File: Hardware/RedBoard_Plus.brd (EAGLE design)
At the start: 68.6 x 58.4 mm, 179 parts, among them IC3 LM1117, J1 DNP, J2 ISP, J3 5.5x2.1mm Barrel, J4 QWIIC_RIGHT_ANGLE, J5 USB Female Type C Connector, Q1 20V/4.2A/52mΩ/1.4W, Q2 310mA/60V/1.6Ω, Q3 310mA/60V/1.6Ω, U1 CH340G, U3 3.3V, U4 ATMEGA328P_TQFP, Y1 16MHz, Y2 12MHz

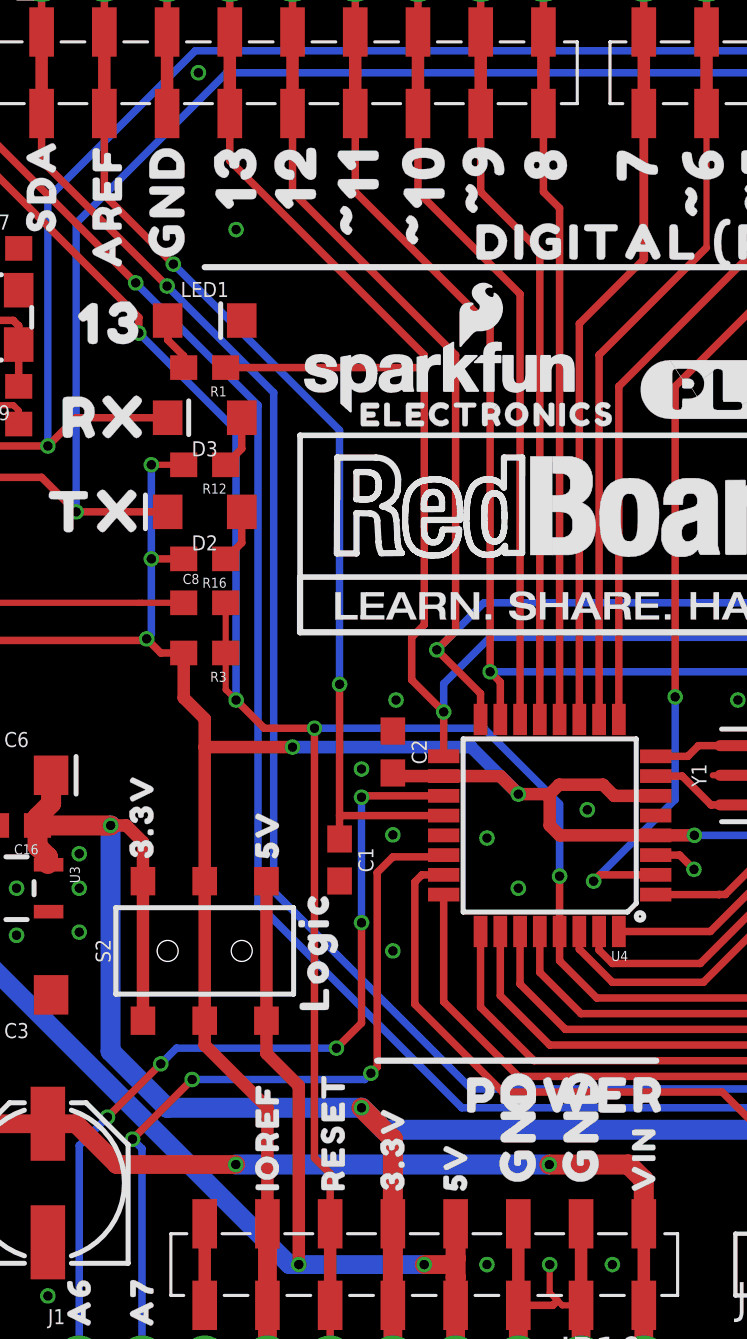
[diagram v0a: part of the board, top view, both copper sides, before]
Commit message: Update "GND" Buzzard labels
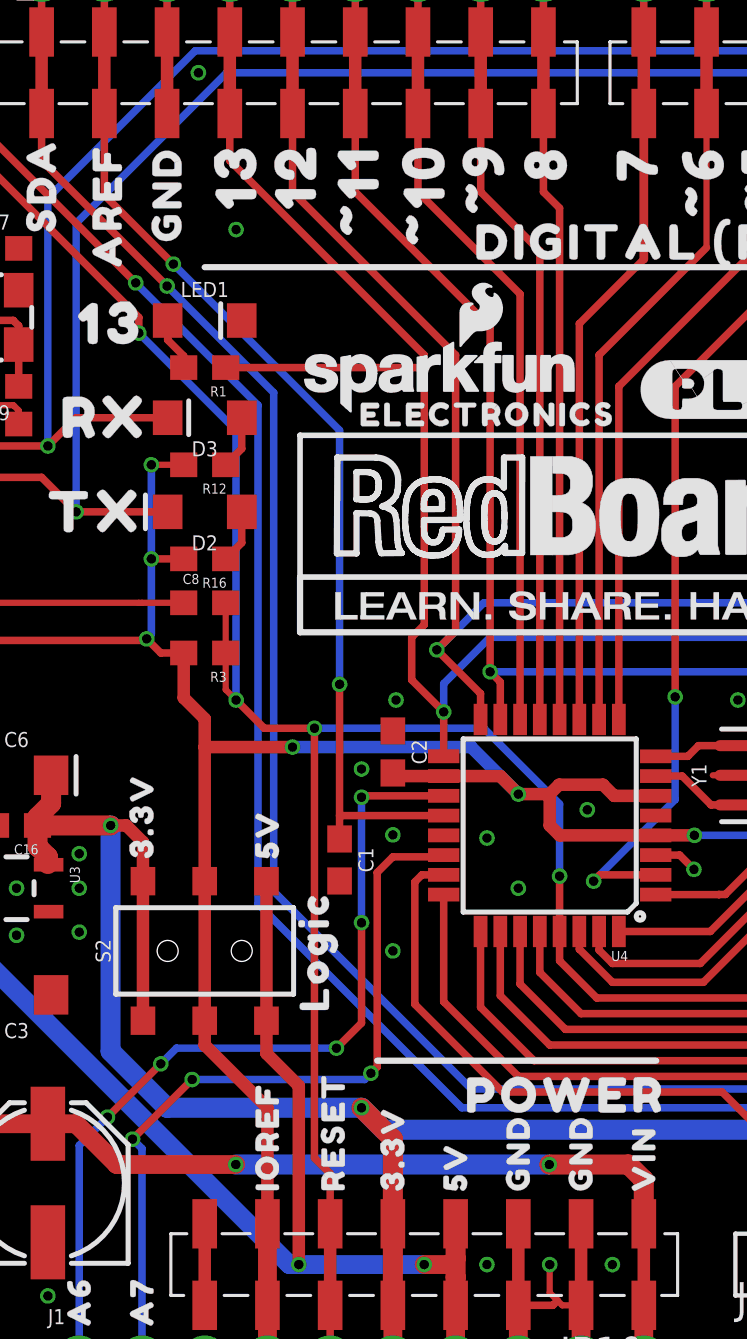
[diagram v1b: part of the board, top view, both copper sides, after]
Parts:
- removed U$21, U$91, U$92: (no value), output:_GND0
- added U$107, U$85: (no value), output:_GND_0
- added U$42: (no value), output:_GND0
- U$99: device output:GND0 -> output:_GND_0
- moved U$99 38.1 mm to (40.6, 9.53), flipped to the bottom, turned to 270 degrees
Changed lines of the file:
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@@
 <?xml version="1.0" encoding="utf-8"?>
 <!DOCTYPE eagle SYSTEM "eagle.dtd">
-<eagle version="9.5.2">
+<eagle version="9.6.2">
 <drawing>
 <settings>
-<setting alwaysvectorfont="no"/>
+<setting alwaysvectorfont="yes"/>
 <setting keepoldvectorfont="yes"/>
 <setting verticaltext="up"/>
@@
 <element name="U$2" library="output" package="_D#0" value="" x="6.096" y="42.799" smashed="yes" rot="MR0"/>
 <element name="U$10" library="output" package="G0" value="" x="5.207" y="39.243" smashed="yes" rot="MR0"/>
-<element name="U$21" library="output" package="_GND0" value="" x="26.416" y="57.658" smashed="yes" rot="MR270"/>
 <element name="FD1" library="SparkFun-Aesthetics" package="FIDUCIAL-1X2" value="FIDUCIAL1X2" x="11.43" y="54.61" smashed="yes" rot="MR0"/>
 <element name="FD2" library="SparkFun-Aesthetics" package="FIDUCIAL-1X2" value="FIDUCIAL1X2" x="66.04" y="13.97" smashed="yes" rot="MR0"/>
@@
 <element name="U$89" library="output" package="_A00" value="" x="50.8" y="7.62" smashed="yes" rot="MR270"/>
 <element name="U$90" library="output" package="_VIN0" value="" x="45.72" y="8.89" smashed="yes" rot="MR270"/>
-<element name="U$91" library="output" package="_GND0" value="" x="43.053" y="9.652" smashed="yes" rot="MR270"/>
-<element name="U$92" library="output" package="_GND0" value="" x="40.64" y="9.652" smashed="yes" rot="MR270"/>
 <element name="U$93" library="output" package="_5V0" value="" x="38.1" y="7.62" smashed="yes" rot="MR270"/>
 <element name="U$94" library="output" package="_3#3V0" value="" x="35.56" y="10.16" smashed="yes" rot="MR270"/>
@@
 <element name="U$98" library="output" package="_A70" value="" x="25.4" y="7.62" smashed="yes" rot="MR270"/>
 <element name="U$13" library="output" package="_RESET0" value="" x="-0.762" y="48.387" smashed="yes"/>
-<element name="U$99" library="output" package="GND0" value="" x="26.416" y="44.831" smashed="yes" rot="R90"/>
 <element name="U$18" library="output" package="_AREF0" value="" x="24.003" y="44.196" smashed="yes" rot="R90"/>
 <element name="U$19" library="output" package="_SCL0" value="" x="18.796" y="45.72" smashed="yes" rot="R90"/>
@@
 <element name="U$106" library="output" package="#A5#0" value="" x="62.611" y="14.732" smashed="yes" rot="MR0"/>
 <element name="U$11" library="output" package="LOGIC0" value="" x="32.385" y="14.478" smashed="yes" rot="R90"/>
+<element name="U$42" library="output" package="_GND0" value="" x="26.416" y="45.212" smashed="yes" rot="R90"/>
+<element name="U$85" library="output" package="_GND_0" value="" x="26.416" y="57.785" smashed="yes" rot="MR270"/>
+<element name="U$99" library="output" package="_GND_0" value="" x="40.64" y="9.525" smashed="yes" rot="MR270"/>
+<element name="U$107" library="output" package="_GND_0" value="" x="43.18" y="9.525" smashed="yes" rot="MR270"/>
 </elements>
 <signals>

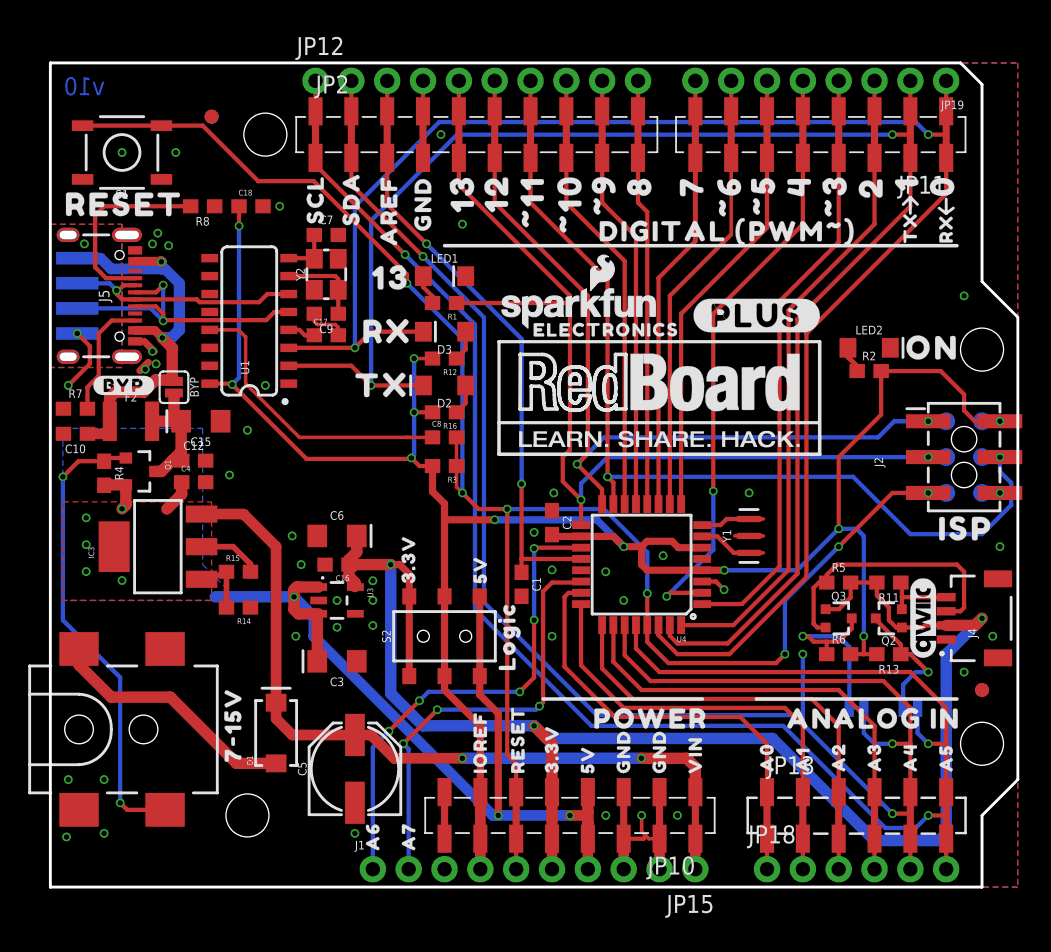
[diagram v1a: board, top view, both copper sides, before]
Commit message: Follow Up review changes
Added Qwiic logo device to schematic
Switch RXO/TXI signals at CH340G. Switched the order of LEDs as well
Updated headers to use current library parts
Updated ISP header sch symbol to use COPI/CIPO
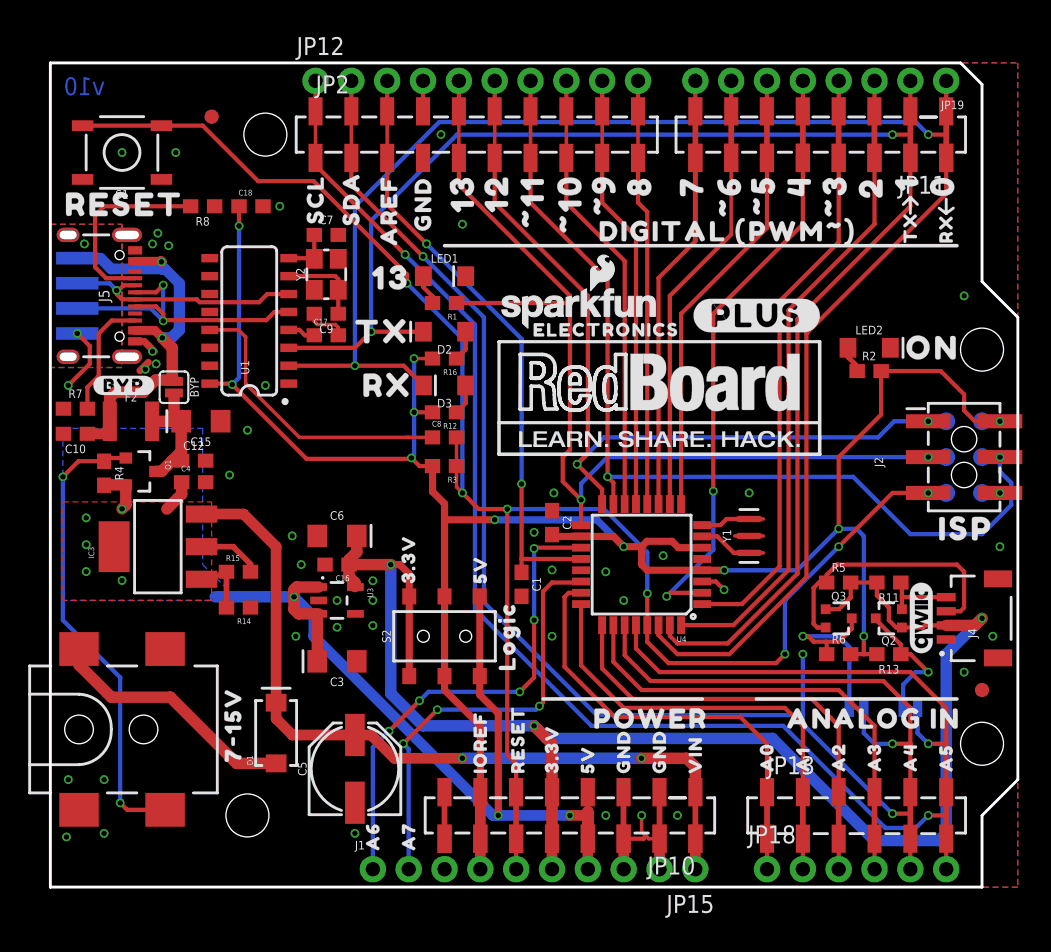
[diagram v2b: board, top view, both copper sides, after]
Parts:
- removed U$9: (no value), Labels:QWIIC_COPYRIGHT_SMALL
- added LOGO1: QWIIC_LOGO_5MM, SparkFun-Aesthetics:QWIIC_5MM
- JP10, JP11: device SparkFun-Connectors:1X08_SMD_COMBINED@1 -> SparkFun-Connectors:1X08_SMD_COMBINED
- JP15: device SparkFun-Connectors:1X08_NO_SILK@1 -> SparkFun-Connectors:1X08_NO_SILK
- JP18: device SparkFun-Connectors:1X06_NO_SILK@1 -> SparkFun-Connectors:1X06_NO_SILK
- JP2: value M10SMD_COMBO -> (none)
- moved R12 3.81 mm to (27.9, 33.7)
- moved R16 3.81 mm to (27.9, 37.5)
- moved D2 3.81 mm to (27.9, 39.4)
- moved D3 3.81 mm to (27.9, 35.6)
- moved U$40 3.81 mm to (19.8, 39.4)
- moved U$41 3.81 mm to (20.3, 35.6)
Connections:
- net !RESET: now also JP10.6; no longer JP10.6A, JP10.6B
- net 3.3V: now also JP10.5; no longer JP10.5A, JP10.5B
- net 5V: now also JP10.4; no longer JP10.4A, JP10.4B
- net A0: now also JP13.1; no longer JP13.1A, JP13.1B
- net A1: now also JP13.2; no longer JP13.2A, JP13.2B
- net A2: now also JP13.3; no longer JP13.3A, JP13.3B
- net A3: now also JP13.4; no longer JP13.4A, JP13.4B
- net A4/SDA: now also JP13.5; no longer JP13.5A, JP13.5B
- net A5/SCL: now also JP13.6; no longer JP13.6A, JP13.6B
- net D2: now also JP11.3; no longer JP11.3A, JP11.3B
- net D3: now also JP11.4; no longer JP11.4A, JP11.4B
- net D4: now also JP11.5; no longer JP11.5A, JP11.5B
- net D5: now also JP11.6; no longer JP11.6A, JP11.6B
- net D6: now also JP11.7; no longer JP11.7A, JP11.7B
- net D7: now also JP11.8; no longer JP11.8A, JP11.8B
- net GND: now also JP10.2, JP10.3; no longer JP10.2A, JP10.2B, JP10.3A, JP10.3B
- net RX-I: now also JP11.1, U1.2; no longer JP11.1A, JP11.1B, U1.3
- net TX-O: now also JP11.2, U1.3; no longer JP11.2A, JP11.2B, U1.2
- net VCC: now also JP10.7; no longer JP10.7A, JP10.7B
- net VIN: now also JP10.1; no longer JP10.1A, JP10.1B
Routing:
- net TX-O: track 114.5 -> 110.6 mm
- net 3.3V: track 114.3 -> 111.0 mm
- net A0: track 35.0 -> 31.7 mm
- net A2: track 34.6 -> 31.7 mm
- net 5V: track 76.2 -> 74.5 mm
- net A4/SDA: track 124.2 -> 122.7 mm
- net RX-I: track 119.4 -> 120.7 mm

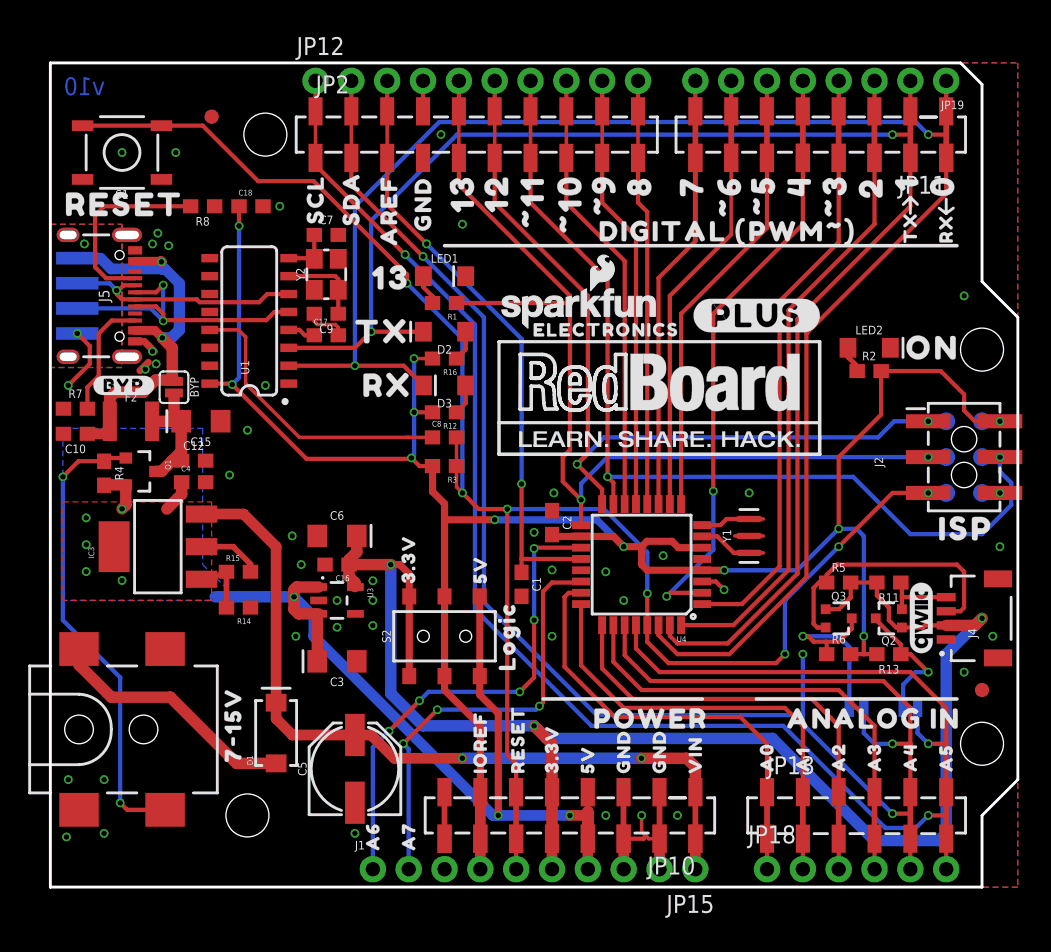
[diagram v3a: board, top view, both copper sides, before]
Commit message: Run engineering checklist
Changes made:
Flipped the V10 on the board edge
Changed the 2 VCC flags in the schematic to power symbols
Added the RedBoard logo to the SF Aesthetics library and replaced the device in the schematic
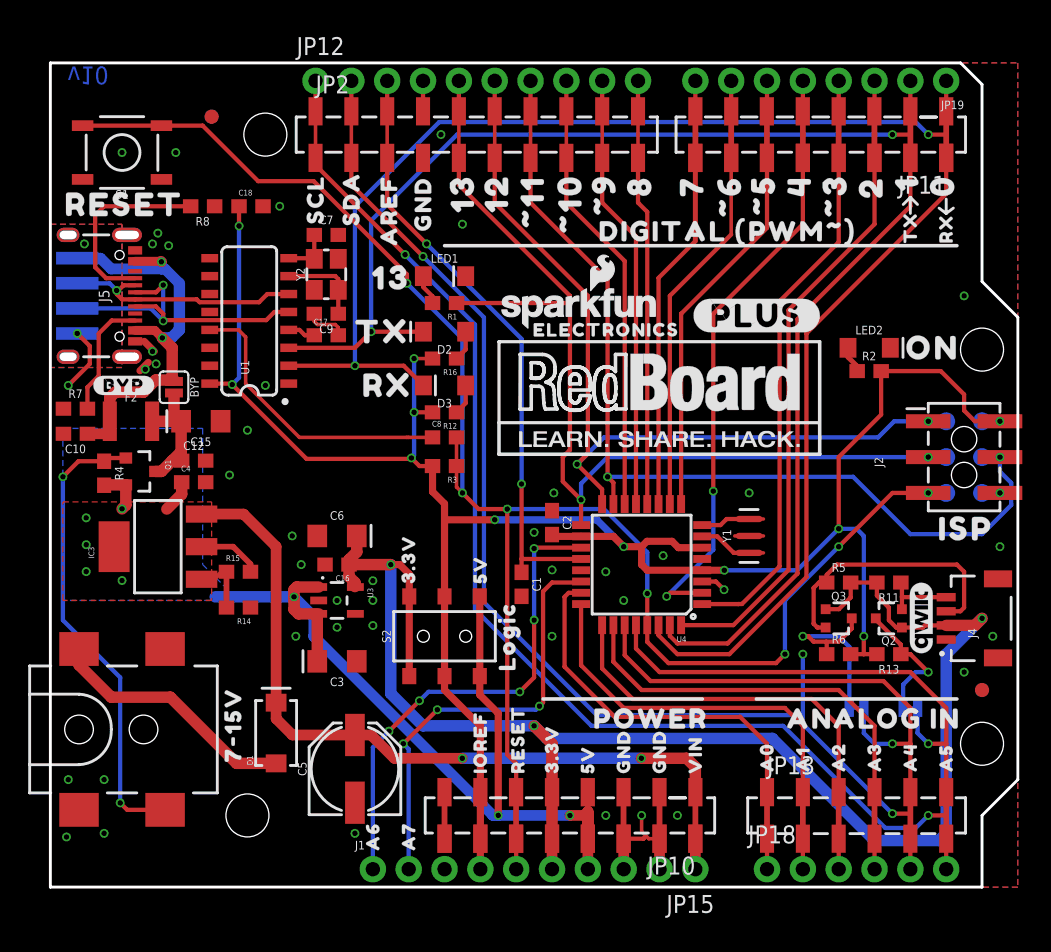
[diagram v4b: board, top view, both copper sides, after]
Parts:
- U$1, U$3: device redboard_logo:REDBOARD_LOGO -> SparkFun-Aesthetics:REDBOARD_LOGO
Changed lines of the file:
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@@
 <wire x1="66.04" y1="56.896" x2="66.04" y2="42.926" width="0.2032" layer="20"/>
 <text x="0" y="-0.0635" size="0.0254" layer="214" font="vector">D:/SmartProjects/Snc/a4_bn_logo2.bmp</text>
-<text x="2.413" y="56.769" size="1.27" layer="16" font="vector" ratio="20" rot="MR0" align="center">v10</text>
+<text x="2.667" y="57.531" size="1.27" layer="16" font="vector" ratio="20" rot="SMR180" align="center">v10</text>
 <rectangle x1="0.635" y1="22.352" x2="2.032" y2="30.607" layer="43"/>
 <rectangle x1="5.715" y1="23.114" x2="7.366" y2="30.607" layer="43"/>
@@
 <element name="FD1" library="SparkFun-Aesthetics" package="FIDUCIAL-1X2" value="FIDUCIAL1X2" x="11.43" y="54.61" smashed="yes" rot="MR0"/>
 <element name="FD2" library="SparkFun-Aesthetics" package="FIDUCIAL-1X2" value="FIDUCIAL1X2" x="66.04" y="13.97" smashed="yes" rot="MR0"/>
-<element name="U$1" library="redboard_logo" package="REDBOARD_LOGO" value="REDBOARD_LOGO" x="31.75" y="30.48" smashed="yes"/>
-<element name="U$3" library="redboard_logo" package="REDBOARD_LOGO" value="REDBOARD_LOGO" x="62.865" y="40.259" smashed="yes" rot="MR0"/>
+<element name="U$1" library="SparkFun-Aesthetics" package="REDBOARD_LOGO" value="REDBOARD_LOGO" x="31.75" y="30.48" smashed="yes"/>
+<element name="U$3" library="SparkFun-Aesthetics" package="REDBOARD_LOGO" value="REDBOARD_LOGO" x="62.865" y="40.259" smashed="yes" rot="MR0"/>
 <element name="U$78" library="SparkFun-Aesthetics" package="SFE_LOGO_NAME_.3" value="" x="33.02" y="26.67" smashed="yes" rot="MR0"/>
 <element name="U$101" library="SparkFun-Aesthetics" package="SFE_LOGO_FLAME_.2" value="" x="29.21" y="31.75" smashed="yes" rot="MR0"/>
@@
 <wire x1="64.77" y1="33.782" x2="64.77" y2="34.925" width="0.3048" layer="1"/>
 <wire x1="66.04" y1="33.02" x2="67.31" y2="33.02" width="0.3048" layer="16"/>
-<contactref element="JP10" pad="7"/>
-<wire x1="30.48" y1="11.43" x2="27.94" y2="13.97" width="0.508" layer="1"/>
-<wire x1="30.48" y1="11.43" x2="30.48" y2="6.73" width="0.508" layer="1"/>
-<wire x1="30.48" y1="3.43" x2="30.48" y2="6.73" width="0.762" layer="1"/>
+<wire x1="27.94" y1="13.97" x2="30.48" y2="11.43" width="0.508" layer="1"/>
 <contactref element="S2" pad="2"/>
 <contactref element="S2" pad="5"/>
@@
 <wire x1="27.94" y1="13.97" x2="27.94" y2="14.955" width="0.508" layer="1"/>
 <wire x1="27.94" y1="20.605" x2="27.94" y2="26.035" width="0.508" layer="1"/>
-<contactref element="JP15" pad="7"/>
-<wire x1="30.48" y1="3.43" x2="30.48" y2="1.27" width="0.762" layer="1"/>
 <contactref element="U1" pad="16"/>
 <wire x1="11.297" y1="35.687" x2="12.827" y2="35.687" width="0.3048" layer="1"/>
@@
 <wire x1="25.781" y1="37.465" x2="27.09" y2="37.465" width="0.254" layer="1"/>
 <wire x1="25.781" y1="33.655" x2="27.09" y2="33.655" width="0.3048" layer="1"/>
+<contactref element="JP10" pad="7"/>
+<contactref element="JP15" pad="7"/>
+<wire x1="30.48" y1="11.43" x2="30.48" y2="3.43" width="0.508" layer="1"/>
+<wire x1="30.48" y1="3.43" x2="30.48" y2="1.27" width="0.508" layer="1"/>
 </signal>
 <signal name="SHLD">
